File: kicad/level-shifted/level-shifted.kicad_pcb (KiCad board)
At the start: 2 copper layers, 54.6 x 49.5 mm, 7 parts, among them J104 PAL-1 Expansion Connector, SW101 PICO RESET, SW102 SW_DIP_x01, U104 Pico

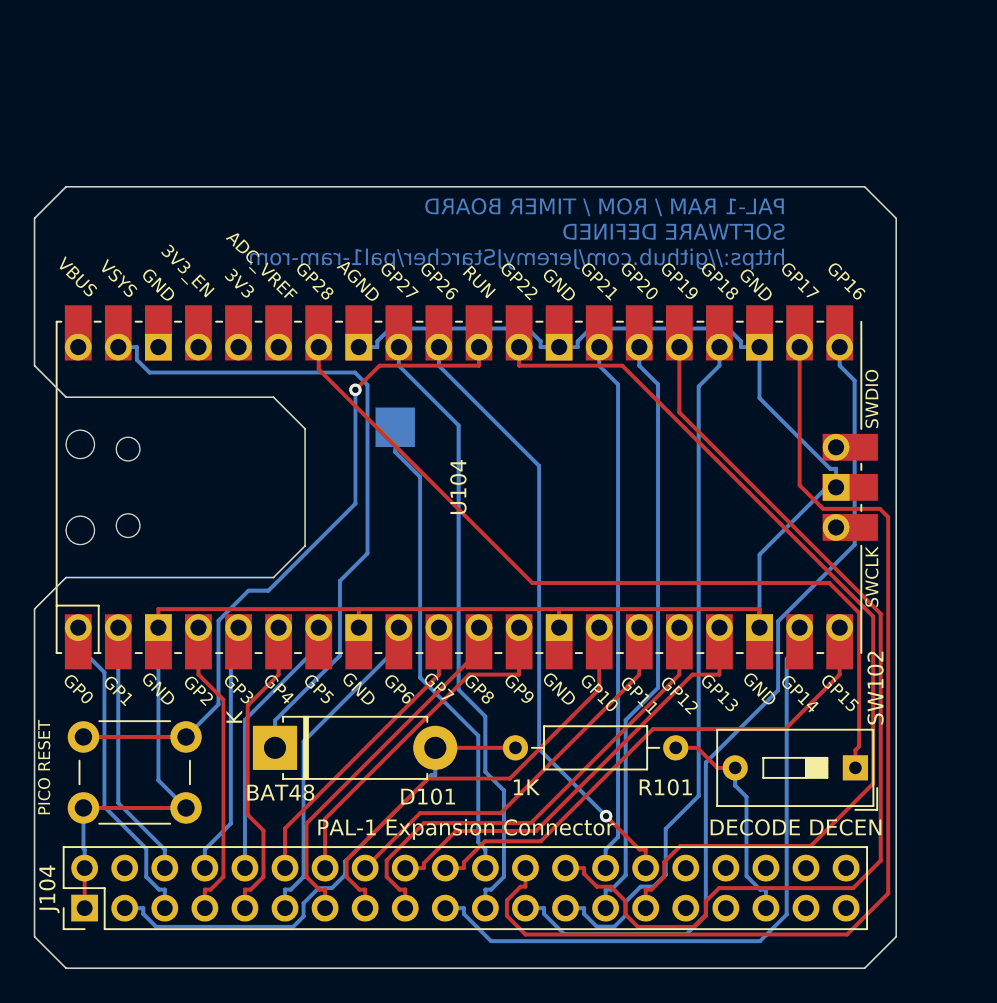
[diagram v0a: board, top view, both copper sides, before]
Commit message: New board prepared with the level shifters in place
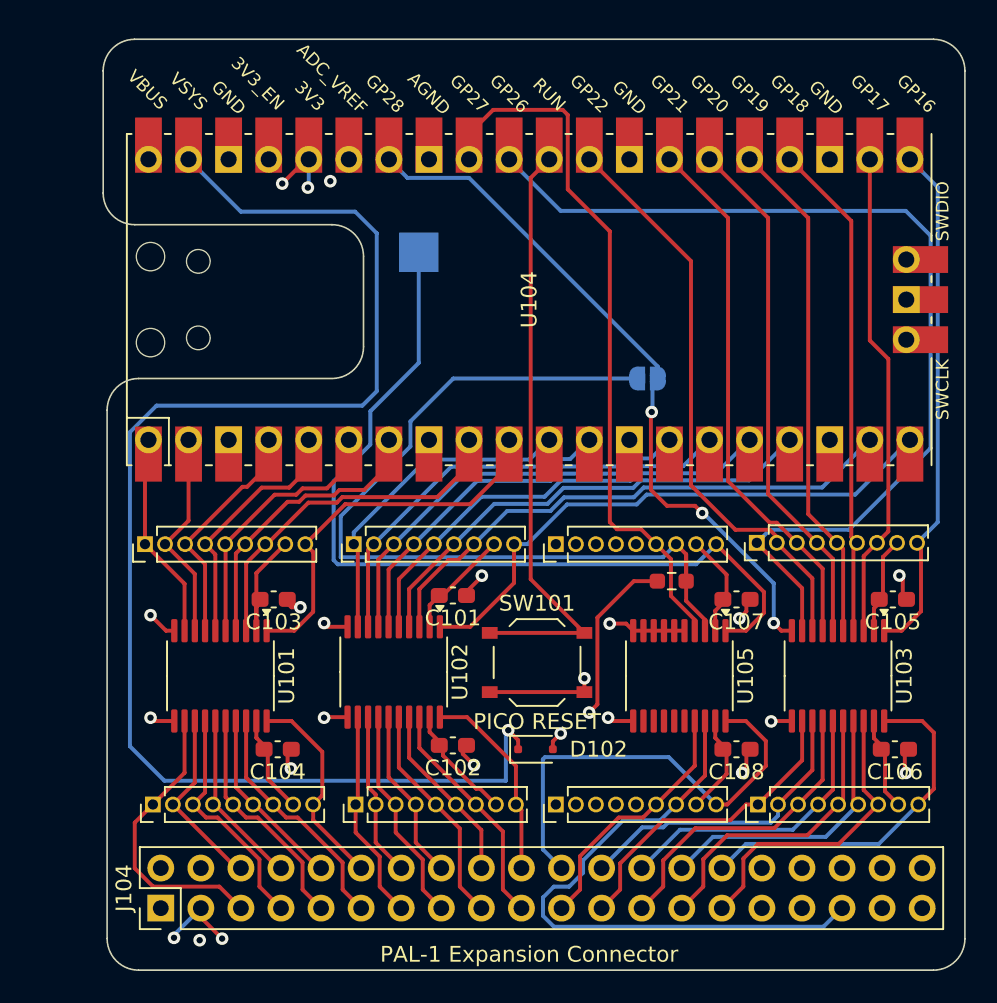
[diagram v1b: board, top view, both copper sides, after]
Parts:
- removed D101: BAT48, Diode_THT:D_5W_P10.16mm_Horizontal
- removed SW102: SW_DIP_x01, Button_Switch_THT:SW_DIP_SPSTx01_Slide_9.78x4.72mm_W7.62mm_P2.54mm
- added C101: 0.1uf, Capacitor_SMD:C_0603_1608Metric_Pad1.08x0.95mm_HandSolder, F.Cu at (147.2, 95.8)
- added C102: 0.1uf, Capacitor_SMD:C_0603_1608Metric_Pad1.08x0.95mm_HandSolder, F.Cu at (147.2, 105.3)
- added C103: 0.1uf, Capacitor_SMD:C_0603_1608Metric_Pad1.08x0.95mm_HandSolder, F.Cu at (135.8, 96.0)
- added C104: 0.1uf, Capacitor_SMD:C_0603_1608Metric_Pad1.08x0.95mm_HandSolder, F.Cu at (136.1, 105.5)
- added C105: 0.1uf, Capacitor_SMD:C_0603_1608Metric_Pad1.08x0.95mm_HandSolder, F.Cu at (175.1, 96.0)
- added C106: 0.1uf, Capacitor_SMD:C_0603_1608Metric_Pad1.08x0.95mm_HandSolder, F.Cu at (175.2, 105.5)
- added C107: 0.1uf, Capacitor_SMD:C_0603_1608Metric_Pad1.08x0.95mm_HandSolder, F.Cu at (165.1, 96.0)
- added C108: 0.1uf, Capacitor_SMD:C_0603_1608Metric_Pad1.08x0.95mm_HandSolder, F.Cu at (165.1, 105.5)
- added D102: 1N4148WS, Diode_SMD:D_SOD-323F, F.Cu at (152.4, 105.5)
- added J101: Conn_01x09_Socket, Connector_PinHeader_1.27mm:PinHeader_1x09_P1.27mm_Vertical, F.Cu at (166.5, 109.0)
- added J102: Conn_01x09_Socket, Connector_PinHeader_1.27mm:PinHeader_1x09_P1.27mm_Vertical, F.Cu at (153.7, 109.0)
- added J103: Conn_01x09_Socket, Connector_PinHeader_1.27mm:PinHeader_1x09_P1.27mm_Vertical, F.Cu at (128.2, 109.0)
- added J105: Conn_01x09_Socket, Connector_PinHeader_1.27mm:PinHeader_1x09_P1.27mm_Vertical, F.Cu at (141.0, 109.0)
- added J106: Conn_01x09_Socket, Connector_PinHeader_1.27mm:PinHeader_1x09_P1.27mm_Vertical, F.Cu at (166.4, 92.4)
- added J107: Conn_01x09_Socket, Connector_PinHeader_1.27mm:PinHeader_1x09_P1.27mm_Vertical, F.Cu at (127.7, 92.5)
- added J109: Conn_01x09_Socket, Connector_PinHeader_1.27mm:PinHeader_1x09_P1.27mm_Vertical, F.Cu at (140.9, 92.5)
- added J110: Conn_01x09_Socket, Connector_PinHeader_1.27mm:PinHeader_1x09_P1.27mm_Vertical, F.Cu at (153.7, 92.5)
- added JP101: DECEN ENABLE, Jumper:SolderJumper-2_P1.3mm_Open_RoundedPad1.0x1.5mm, B.Cu at (159.5, 82.0)
- added U101: TXS0108EPW, Package_SO:TSSOP-20_4.4x6.5mm_P0.65mm, F.Cu at (132.4, 100.8)
- added U102: TXS0108EPW, Package_SO:TSSOP-20_4.4x6.5mm_P0.65mm, F.Cu at (143.4, 100.6)
- added U103: TXS0108EPW, Package_SO:TSSOP-20_4.4x6.5mm_P0.65mm, F.Cu at (171.6, 100.8)
- added U105: TXS0108EPW, Package_SO:TSSOP-20_4.4x6.5mm_P0.65mm, F.Cu at (161.5, 100.8)
- R101: footprint Resistor_THT:R_Axial_DIN0207_L6.3mm_D2.5mm_P10.16mm_Horizontal -> Resistor_SMD:R_0603_1608Metric_Pad0.98x0.95mm_HandSolder
- SW101: footprint Button_Switch_THT:SW_PUSH_6mm -> Button_Switch_SMD:SW_Push_1P1T_XKB_TS-1187A
- moved SW101 29.1 mm to (152.5, 100.0)
- moved R101 14.5 mm to (161.0, 94.8)
- moved U104 12.7 mm to (152.0, 77.0)
- moved TP101 11.2 mm to (145.0, 74.0)
- moved J104 4.83 mm to (128.7, 115.6)
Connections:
- net V5 renamed 5V
- J104 pad 10: A5 -> /HVA5
- J104 pad 11: A6 -> /HVA6
- J104 pad 12: A7 -> /HVA7
- J104 pad 13: A8 -> /HVA8
- J104 pad 14: A9 -> /HVA9
- J104 pad 15: A10 -> /HVA10
- J104 pad 16: A11 -> /HVA11
- J104 pad 17: A12 -> /HVA12
- J104 pad 18: A13 -> /HVA13
- J104 pad 19: A14 -> /HVA14
- J104 pad 20: A15 -> /HVA15
- J104 pad 21: RW -> HVRW
- J104 pad 22: PHI2 -> HVPHI2
- J104 pad 23: D0 -> HVD0
- J104 pad 24: D1 -> HVD1
- J104 pad 25: D2 -> HVD2
- J104 pad 26: D3 -> HVD3
- J104 pad 27: D4 -> HVD4
- J104 pad 28: D5 -> HVD5
- J104 pad 29: D6 -> HVD6
- J104 pad 30: D7 -> HVD7
- J104 pad 35: DEN -> HVDEN
- J104 pad 5: A0 -> /HVA0
- J104 pad 6: A1 -> /HVA1
- J104 pad 7: A2 -> /HVA2
- J104 pad 8: A3 -> /HVA3
- J104 pad 9: A4 -> /HVA4
- R101 pad 2: DEN -> LVDEN
- TP101 pad 1: PHI2 -> LVPHI2
- U104 pad 1: A0 -> /LVA0
- U104 pad 10: A7 -> /LVA7
- U104 pad 11: A8 -> /LVA8
- U104 pad 12: A9 -> /LVA9
- U104 pad 14: A10 -> /LVA10
- U104 pad 15: A11 -> /LVA11
- U104 pad 16: A12 -> /LVA12
- U104 pad 17: A13 -> /LVA13
- U104 pad 19: A14 -> /LVA14
- U104 pad 2: A1 -> /LVA1
- U104 pad 20: A15 -> /LVA15
- U104 pad 21: D0 -> LVD7
- U104 pad 22: D1 -> LVD6
- U104 pad 24: D2 -> LVD5
- U104 pad 25: D3 -> LVD4
- U104 pad 26: D4 -> LVD3
- U104 pad 27: D5 -> LVD2
- U104 pad 29: D6 -> LVD1
- U104 pad 31: D7 -> LVD0
- U104 pad 32: RW -> LVRW
- U104 pad 34: Net-(U104-GPIO28_ADC2) -> /DEN
- U104 pad 36: V3.3 -> 3V3
- U104 pad 4: A2 -> /LVA2
- U104 pad 5: A3 -> /LVA3
- U104 pad 6: A4 -> /LVA4
- U104 pad 7: A5 -> /LVA5
- U104 pad 9: A6 -> /LVA6
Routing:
- net GND: track 118.7 -> 25.0 mm, vias 0 -> 13
- net D1: track 68.5 -> 0.00 mm
- net LVD0: track 0.00 -> 62.4 mm
- net D3: track 62.3 -> 0.00 mm
- net D6: track 59.7 -> 0.00 mm
- net LVDEN: track 0.00 -> 55.8 mm
- net LVPHI2: track 0.00 -> 55.1 mm
- net D0: track 53.1 -> 0.00 mm
- net Net-(U104-GPIO28_ADC2): track 52.0 -> 0.00 mm
- net Net-(D102-K): track 42.7 -> 90.0 mm, vias 0 -> 1
- net LVRW: track 0.00 -> 45.6 mm
- net /DEN: track 0.00 -> 44.6 mm, vias 0 -> 3
- net D2: track 43.8 -> 0.00 mm
- net 3V3: track 0.00 -> 42.7 mm, vias 0 -> 6
- net A14: track 41.9 -> 0.00 mm
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- added copper zone on In2.Cu, net 3V3
- added copper zone on In2.Cu, net 5V
- added copper zone on In1.Cu, net GND
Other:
- board size 54.6 x 49.5 mm -> 54.6 x 59 mm
- copper layers 2 -> 4
- board text removed: "ONLY ONE BOARD ON THE BUS CAN DECODE DECEN TO ENABLE THE PAL-1s ADDRESS INTERNAL ADDRESSING"

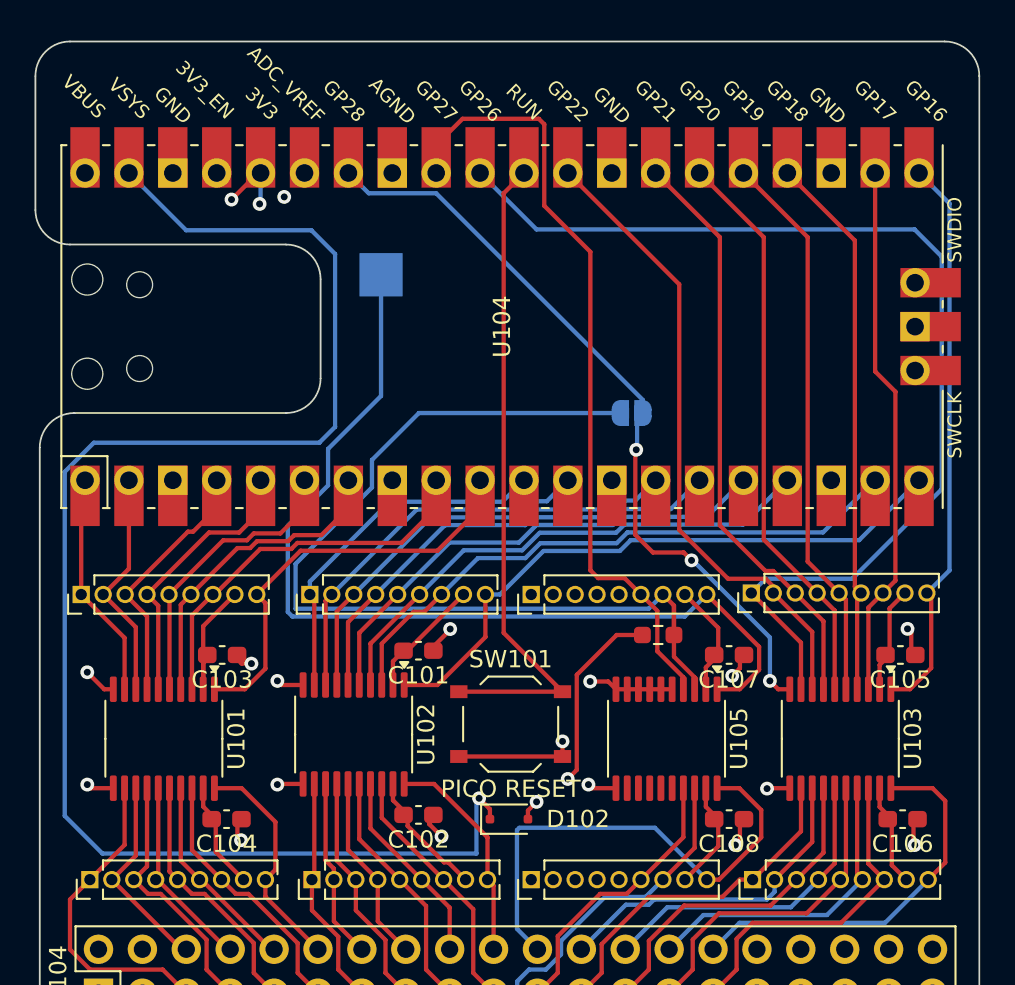
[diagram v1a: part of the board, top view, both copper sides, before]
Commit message: Updated the PCB to use the old (normal) pin numberings and ordered the board
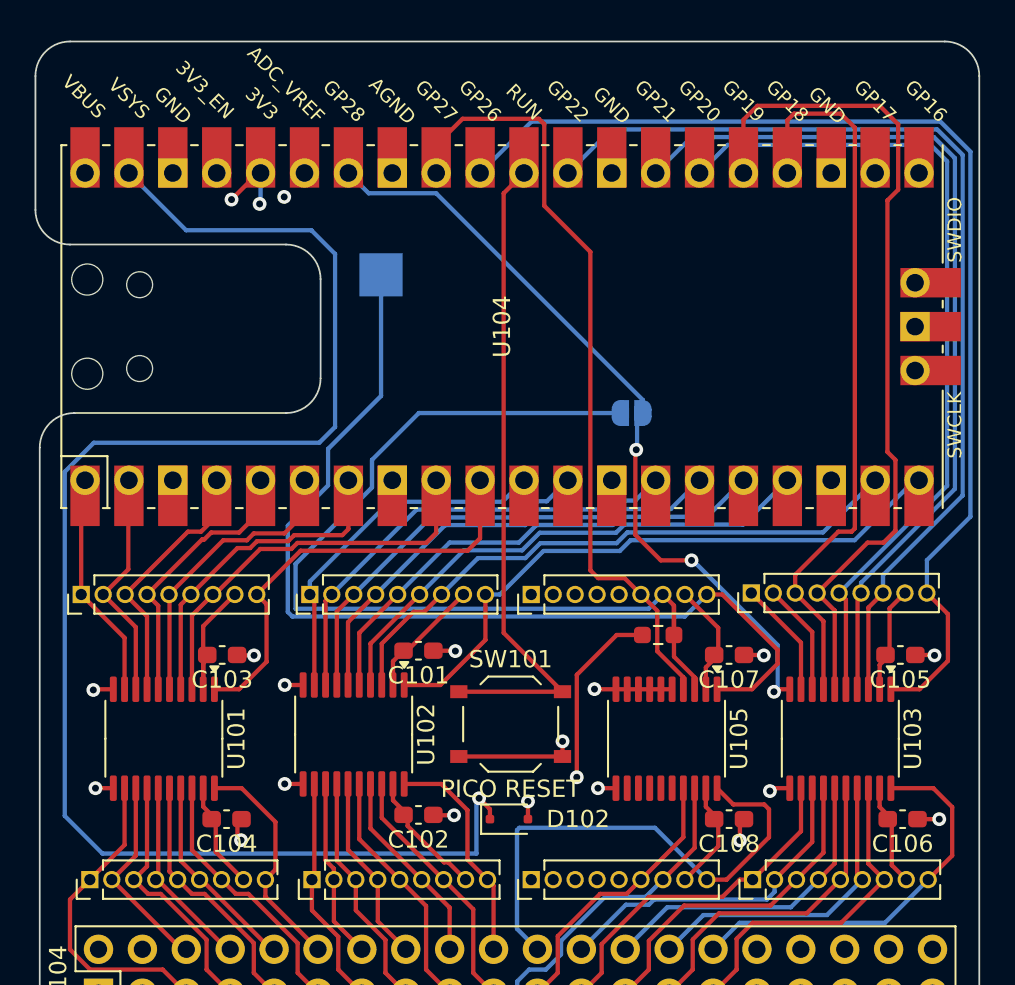
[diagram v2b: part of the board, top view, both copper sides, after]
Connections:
- U104 pad 21: LVD7 -> LVD0
- U104 pad 22: LVD6 -> LVD1
- U104 pad 24: LVD5 -> LVD2
- U104 pad 25: LVD4 -> LVD3
- U104 pad 26: LVD3 -> LVD4
- U104 pad 27: LVD2 -> LVD5
- U104 pad 29: LVD1 -> LVD6
- U104 pad 31: LVD0 -> LVD7
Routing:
- net LVD7: track 32.9 -> 65.3 mm
- net LVD6: track 31.0 -> 57.7 mm
- net LVD0: track 62.4 -> 40.0 mm
- net LVD5: track 31.7 -> 51.8 mm
- net LVD4: track 32.3 -> 48.7 mm
- net LVD3: track 33.1 -> 48.8 mm
- net LVD2: track 34.2 -> 42.5 mm
- net LVD1: track 37.0 -> 44.6 mm
- net GND: track 25.0 -> 22.2 mm
- net LVPHI2: track 55.1 -> 57.0 mm
- net 3V3: track 42.7 -> 41.1 mm
- net HVPHI2: track 28.5 -> 29.4 mm
- net /LVA7: track 24.5 -> 25.4 mm
- net /LVA6: track 22.6 -> 23.4 mm
- net /LVA5: track 18.5 -> 19.2 mm
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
